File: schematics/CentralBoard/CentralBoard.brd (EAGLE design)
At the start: 100 x 80 mm, 10 parts, among them CON1 XT30UPB-M, CON3 XT30UPB-M, IC1 7805T

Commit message: Starting schematics
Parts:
- removed JP1: OD0_Serial, adafruit:1X03
- added C10, C11, C12, C13, C14, C15, C9: 2.2uF, rcl:C1206
- added C17, C2, C4, C7: 100nF, rcl:C0805
- added CON2, CON4, CON5, CON6, CON7, CON8: XT30UPB-M, amass:XT30UPB-M
- added F1: Fuse 0.2A, fuse:SHK20L
- added IC2: SN75C3232, MAX3232:SOIC16
- added IC3: LTC7001, LTC7001:MSOP10
- added Q1: BC328, transistor-pnp:TO92-EBC
- added R3: 4m, rcl:R2512
- added R4: 10K, rcl:R0805
- added R5: 100K, rcl:R0805
- added R6, R7: 1K, rcl:R0805
- added SJ1, SJ2, SJ3, SJ4: 0, jumper:SJ
- added SV3: IMU, con-lstb:MA06-1
- added U$2: NVMFS6H824NL-D, DIO_NTS1045EMFST1G:DIO_NTS1045EMFST1G
- C1: value (none) -> 1uF; device rcl:E15-5 -> rcl:E2-5
- C3: value (none) -> 4.7uF; device rcl:E15-5 -> rcl:C0805
- C5: value (none) -> 10uF; device rcl:E2,5-7 -> rcl:E2-5
- C6: value (none) -> 0.47uF; device rcl:E2,5-7 -> rcl:C0805
- D1: device adafruit:DO41-10 -> diode:DO41-10
- IC1: value 7805T -> R-78C05.0; device adafruit:TO220H -> v-reg:78XXS
- moved CON3 166.9 mm to (12.7, 86.4)
- moved IC1 162.9 mm to (152.4, 35.6)
- moved C5 155.4 mm to (100.3, 68.6)
- moved CON1 151.8 mm to (12.7, 94.0)
- moved C6 139.3 mm to (44.5, 81.3)
- moved C1 128.1 mm to (91.4, 68.6)
- moved D1 113.7 mm to (88.9, 52.1)
- moved C3 108.6 mm to (44.5, 69.8)
- moved U$1 51.5 mm to (99.1, 17.8)
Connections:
- removed net RX1: JP1.1, U$1.0-RX1/CS1/CRX2
- removed net TX1: JP1.2, U$1.1-TX1/MISO1/CTX2
- new net +5V: C5.+, D1.A, IC1.OUT, IC3.1, Q1.E, R6.1, U$1.VIN
- new net BATT+: CON1.+, CON3.+, R3.1, SJ1.1
- new net BATT-: C10.2, C11.2, C12.2, C13.2, C14.2, C15.2, C9.2, CON1.-, CON2.-, CON3.-, CON4.-, CON5.-, CON6.-, CON7.-, CON8.-, SJ2.1, SJ4.2
- new net IMU-D+: SV3.4
- new net IMU_D-: SV3.3
- new net IMU_RX: IC2.P$14, SV3.6
- new net IMU_TX: IC2.P$13, SV3.5
- new net IMU_VDD: Q1.C, SV3.2
- new net N$1: C1.+, D1.C, F1.2A, IC1.IN
- new net N$10: IC3.4, R4.2, U$1.30-CRX3
- new net N$11: C2.1, IC2.P$4
- new net N$12: C2.2, IC2.P$5
- new net N$13: C7.1, IC2.P$2
- new net N$14: C4.1, IC2.P$6
- new net N$15: R4.1, SJ4.1
- new net N$16: C3.1, IC3.9
- new net N$17: IC3.7, R5.2
- new net N$18: R3.2, U$2.5_6
- new net N$19: C6.1, IC3.6, R5.1, U$2.4
- new net N$2: IC2.P$11, U$1.29-TX7
- new net N$20: F1.1A, SJ1.2
- new net N$21: C10.1, C11.1, C12.1, C13.1, C14.1, C15.1, C9.1, CON2.+, CON4.+, CON5.+, CON6.+, CON7.+, CON8.+, SJ3.2, U$2.1, U$2.2, U$2.3
- new net N$5: IC2.P$12, U$1.28-RX7
- new net N$6: C17.1, IC2.P$1
- new net N$7: R6.2, R7.1, U$1.10-CS\MQSR
- new net N$8: C17.2, IC2.P$3
- new net N$9: IC2.P$16, U$1.3V3-3
- net GND: now also C4.2, C7.2, IC1.GND, IC2.P$15, IC3.11, IC3.2, IC3.3, IC3.5, SJ2.2, SV3.1; no longer C3.-, C6.-, CON1.-, CON3.-, IC1.2, JP1.3
- net N$3: now also Q1.B, R7.2; no longer C1.+, C5.+, D1.A, IC1.3, U$1.VIN
- net N$4: now also C3.2, C6.2, IC3.8, SJ3.1; no longer C3.+, C6.+, CON1.+, CON3.+, D1.C, IC1.1
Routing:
- net GND: track 0.00 -> 294.1 mm, vias 0 -> 1
- net +5V: track 0.00 -> 195.5 mm, vias 0 -> 2
- net N$1: track 0.00 -> 134.0 mm
- net BATT-: track 0.00 -> 122.2 mm
- net N$10: track 0.00 -> 103.4 mm, vias 0 -> 1
- net N$20: track 0.00 -> 92.3 mm
- net N$21: track 0.00 -> 86.9 mm, vias 0 -> 1
- net N$7: track 0.00 -> 81.7 mm
- net N$3: track 0.00 -> 70.4 mm
- net N$6: track 0.00 -> 67.2 mm, vias 0 -> 2
- net N$8: track 0.00 -> 66.9 mm, vias 0 -> 2
- net N$13: track 0.00 -> 48.2 mm, vias 0 -> 2
- net N$15: track 0.00 -> 46.4 mm
- net N$5: track 0.00 -> 41.9 mm
- net N$19: track 0.00 -> 40.5 mm
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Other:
- board size 100 x 80 mm -> 160 x 100 mm

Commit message: used MAX3232 IC for IMU connection now
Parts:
- removed C3: 4.7uF, rcl:C0805
- removed F1: Fuse 0.2A, fuse:SHK20L
- removed IC3: LTC7001, LTC7001:MSOP10
- removed R5: 100K, rcl:R0805
- removed R6: 1K, rcl:R0805
- added D2: 1N4148DO35-7, diode:DO35-7
- added R1: 10k, rcl:R0805
- added U1: LTC4440ES6-5TRMSOP8P, LTC4440ES6-5TR:MSOP8P
- U$2: value NVMFS6H824NL-D -> DMTH8003SPS
- moved C17 59.9 mm to (104.1, 33.0)
- moved C7 54.6 mm to (99.1, 33.0)
- moved Q1 17.7 mm to (150.5, 48.9)
- moved IC1 11.8 mm to (142.9, 42.5)
- moved C4 5.24 mm to (114.3, 33.0)
- moved IC2 2.54 mm to (106.7, 40.6)
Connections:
- removed net N$16: C3.1, IC3.9
- removed net N$17: IC3.7, R5.2
- new net N$24: C6.1, D2.C, U1.6
- net +5V: now also D2.A, R1.1, U1.3; no longer IC3.1, R6.1
- net GND: no longer IC3.11, IC3.2, IC3.3, IC3.5
- net N$1: no longer F1.2A
- net N$10: now also U1.1; no longer IC3.4
- net N$15: now also U1.2, U1.4, U1.9
- net N$19: now also U1.7; no longer C6.1, IC3.6, R5.1
- net N$20: no longer F1.1A
- net N$3: now also R1.2
- net N$4: now also U1.8; no longer C3.2, IC3.8
- net N$7: now also U$1.9-OUT1C; no longer R6.2, U$1.10-CS\MQSR
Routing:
- net GND: track 294.1 -> 0.00 mm, vias 1 -> 0
- net +5V: track 195.5 -> 0.00 mm, vias 2 -> 0
- net N$1: track 134.0 -> 0.00 mm
- net BATT-: track 122.2 -> 0.00 mm
- net N$10: track 103.4 -> 0.00 mm, vias 1 -> 0
- net N$20: track 92.3 -> 0.00 mm
- net N$21: track 86.9 -> 0.00 mm, vias 1 -> 0
- net N$7: track 81.7 -> 0.00 mm
- net N$3: track 70.4 -> 0.00 mm
- net N$6: track 67.2 -> 0.00 mm, vias 2 -> 0
- net N$8: track 66.9 -> 0.00 mm, vias 2 -> 0
- net N$13: track 48.2 -> 0.00 mm, vias 2 -> 0
- net N$15: track 46.4 -> 0.00 mm
- net N$5: track 41.9 -> 0.00 mm
- net N$19: track 40.5 -> 0.00 mm
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
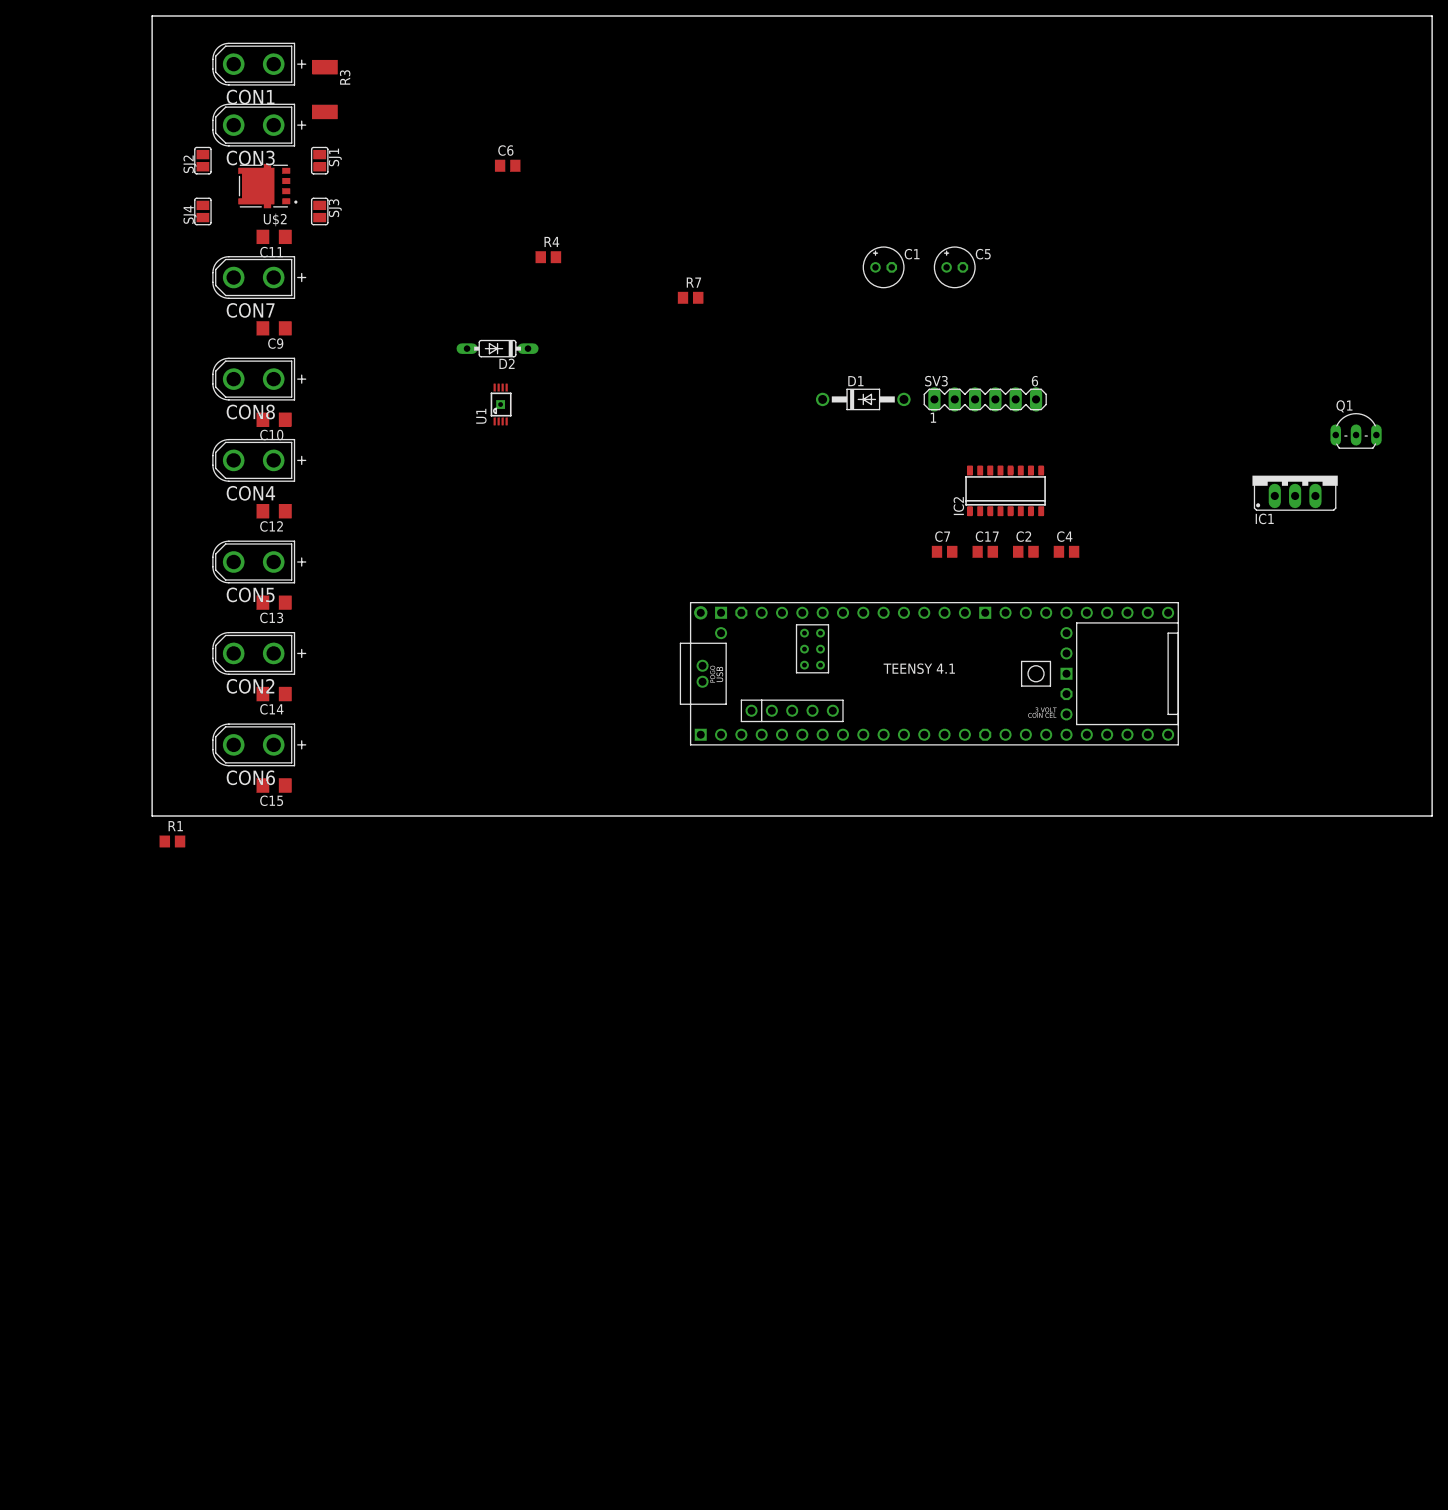
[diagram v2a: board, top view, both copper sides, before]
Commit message: Added sockets for IMU, Sensors and ODrives
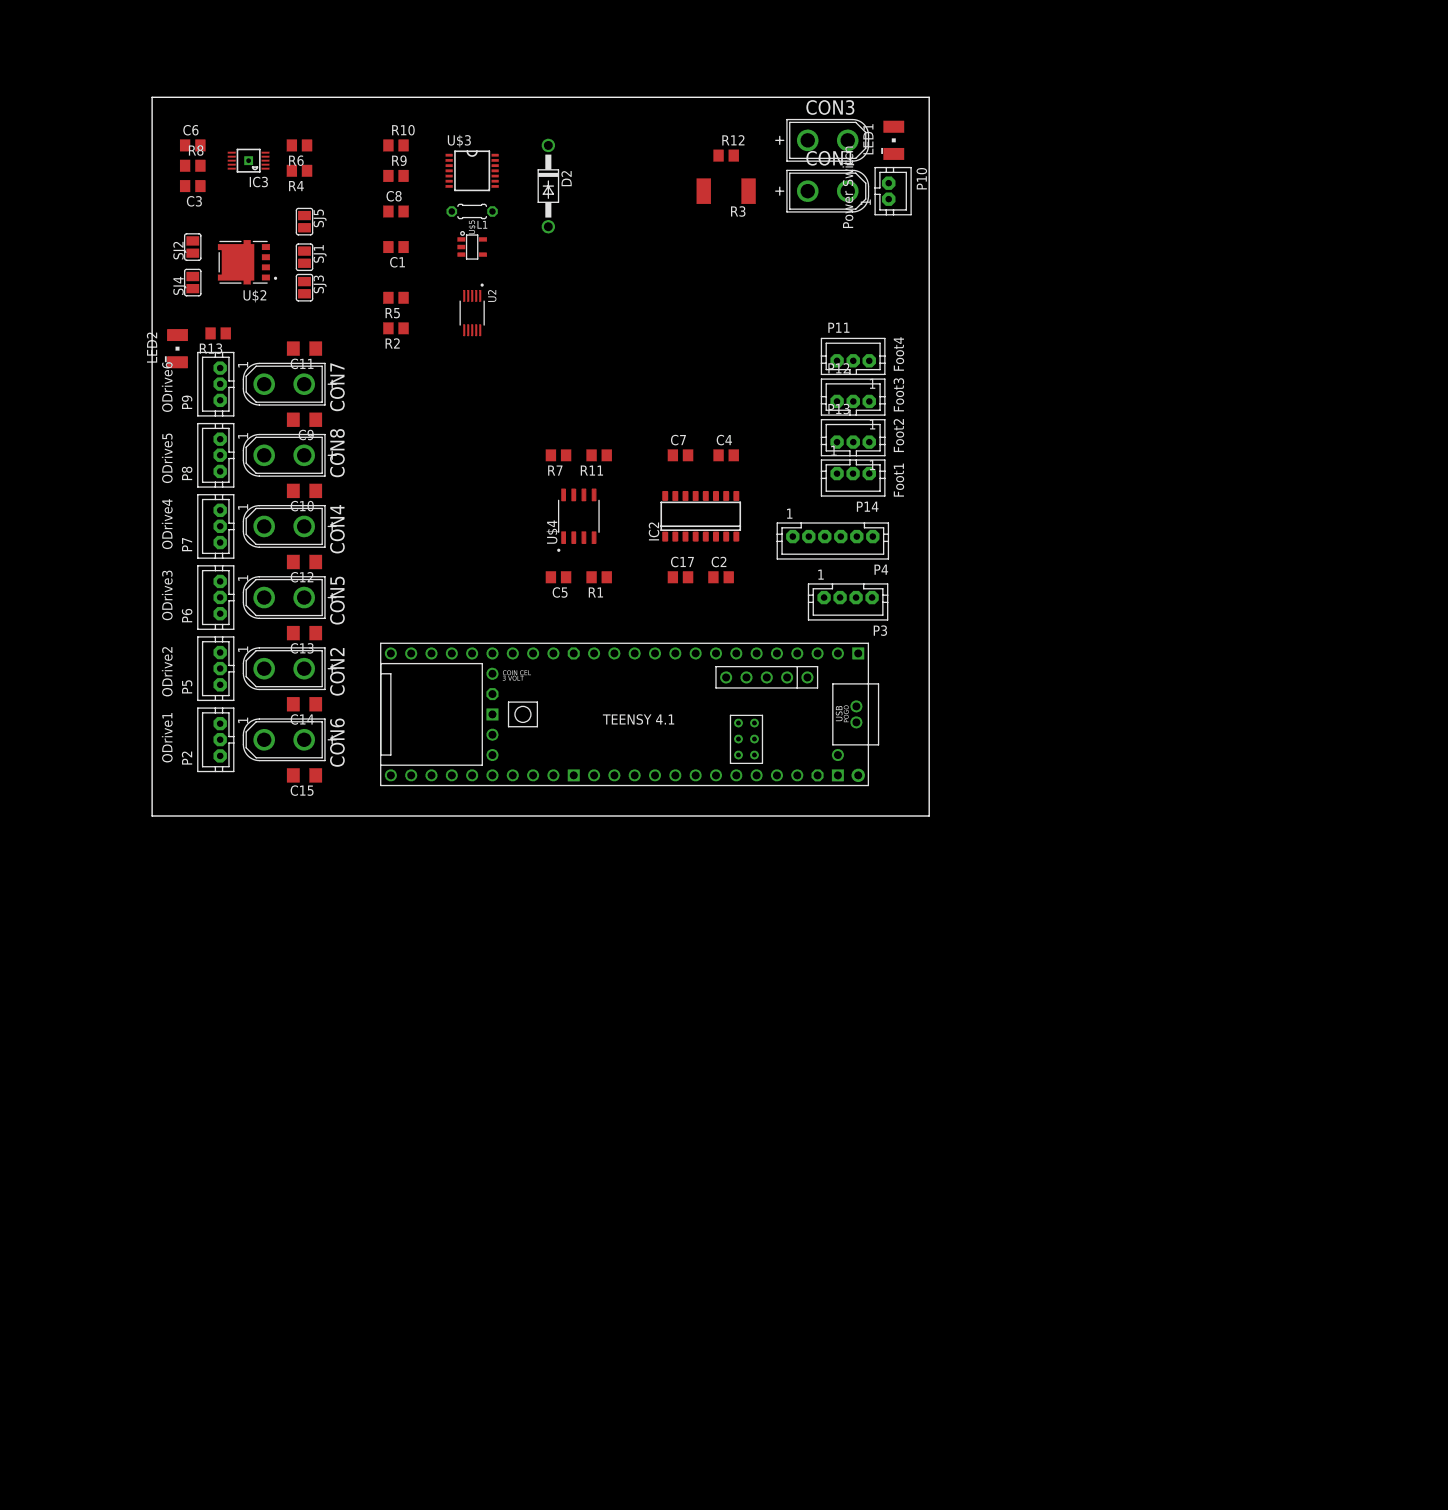
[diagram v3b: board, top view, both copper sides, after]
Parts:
- removed D1: 1N4004, diode:DO41-10
- removed IC1: R-78C05.0, v-reg:78XXS
- removed Q1: BC328, transistor-pnp:TO92-EBC
- removed SV3: IMU, con-lstb:MA06-1
- removed U1: LTC4440ES6-5TRMSOP8P, LTC4440ES6-5TR:MSOP8P
- added C3: 4.7uF, rcl:C0805
- added C8: 10uF, rcl:C0805
- added IC3: LTC7001, LTC7001:MSOP10
- added L1: 10uH, rcl:0204/5
- added LED1: Power, led:PLCC2
- added LED2: P-ODrive, led:PLCC2
- added P10: Power Switch, jst-ph:JST-PH2
- added P11: Foot4, jst-ph:JST-PH3
- added P12: Foot3, jst-ph:JST-PH3
- added P13: Foot2, jst-ph:JST-PH3
- added P14: Foot1, jst-ph:JST-PH3
- added P2: ODrive1, jst-ph:JST-PH3
- added P3: MAIN_SPI, jst-ph:JST-PH4
- added P4: IMU, jst-ph:JST-PH6
- added P5: ODrive2, jst-ph:JST-PH3
- added P6: ODrive3, jst-ph:JST-PH3
- added P7: ODrive4, jst-ph:JST-PH3
- added P8: ODrive5, jst-ph:JST-PH3
- added P9: ODrive6, jst-ph:JST-PH3
- added R10: 100k, rcl:R0805
- added R11, R8: 100K, rcl:R0805
- added R12, R13: 1K, rcl:R0805
- added R2, R5: 2.2K, rcl:R0805
- added R6: 10K, rcl:R0805
- added R9: 47k, rcl:R0805
- added SJ5: 0, jumper:SJ
- added U$3: TLF50211EL, TLF50211EL:TSSOP-14
- added U$4: MCP1725-ADJE/SN, MCP1725-ADJE_SN:SOIC127P599X175-8N
- added U$5: AP2128-3.3V, AP2128:SOT-23-5
- added U2: INA226AIDGST, INA226AIDGST:SOP50P490X110-10N
- C1: device rcl:E2-5 -> rcl:C0805
- C5: value 10uF -> 1nF; device rcl:E2-5 -> rcl:C0805
- D2: value 1N4148DO35-7 -> 1N4004; device diode:DO35-7 -> diode:DO41-10
- R1: value 10k -> 100K
- R7: value 1K -> 10K
- moved CON1 73.5 mm to (84.5, 78.1), turned to 180 degrees
- moved CON3 71.8 mm to (84.5, 84.5), turned to 180 degrees
- moved C5 62.9 mm to (50.8, 29.8), turned to 180 degrees
- moved R1 62.7 mm to (55.9, 29.8), turned to 180 degrees
- moved C1 61.0 mm to (30.5, 71.1), turned to 180 degrees
- moved R3 51.7 mm to (71.8, 78.1), turned to 180 degrees
- moved C4 44.2 mm to (71.8, 45.1)
- moved U$1 41.6 mm to (57.8, 12.7), turned to 180 degrees
- moved C6 39.5 mm to (5.08, 83.8)
- moved IC2 38.2 mm to (68.6, 37.5)
- moved C17 38.2 mm to (66.0, 29.8)
- moved C2 38.2 mm to (71.1, 29.8)
- moved C7 35.2 mm to (66.0, 45.1)
- moved R4 32.9 mm to (18.4, 80.6), turned to 180 degrees
- moved R7 25.7 mm to (50.8, 45.1), turned to 180 degrees
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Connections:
- net N$2 renamed T_TX
- net N$5 renamed T_RX
- new net +3.3V: C1.1, P11.2, P12.2, P13.2, P14.2, U$5.4
- new net BATT: P10.1, SJ1.2, U$3.13, U2.10, U2.8
- new net CS: P3.4, U$1.10-CS\MQSR
- new net MISO: P3.2, U$1.12-MISO/MQSL
- new net MOSI: P3.3, U$1.11-MOSI/CTX1
- new net N$16: C6.2, R6.2
- new net N$17: R2.1, U$1.19-A5/SCL0, U2.5
- new net N$2: LED1.C, R12.2
- new net N$22: R5.1, U$1.18-A4/SDA0, U2.4
- new net N$23: R11.2, R2.2, R5.2, U$1.3V3-3, U2.6
- new net N$25: R1.1, R7.2, U$4.7
- new net N$26: C3.2, IC3.8, LED2.A, SJ3.1
- new net N$27: R9.2, U$3.5
- new net N$29: D2.C, L1.1, U$3.11
- new net N$30: LED2.C, R13.2
- new net N$31: IC2.P$16, P4.5, R1.2, U$4.8
- new net N$5: U$1.31-CTX3, U2.3
- new net O1_RX: P2.2, U$1.0-RX1/CS1/CRX2
- new net O1_TX: P2.3, U$1.1-TX1/MISO1/CTX2
- new net O2_RX: P5.2, U$1.7-RX2/OUT1A
- new net O2_TX: P5.3, U$1.8-TX2/IN1
- new net O3_RX: P6.2, U$1.15-A1/RX3/SPDIF_IN
- new net O3_TX: P6.3, U$1.14-A0/TX3/SPDIF_OUT
- new net O4_RX: P7.2, U$1.16-A2/RX4/SCL1
- new net O4_TX: P7.3, U$1.17-A3/TX4/SDA1
- new net O5_RX: P8.2, U$1.21-A7/RX5/BCLK1
- new net O5_TX: P8.3, U$1.20-A6/TX5/LRCLK1
- new net O6_RX: P9.2, U$1.25-A11/RX6/SDA2
- new net O6_TX: P9.3, U$1.24-A10/TX6/SCL2
- new net SENSOR1: P14.3, U$1.22-A8/CTX1
- new net SENSOR2: P13.3, U$1.23-A9/CRX1/MCLK1
- new net SENSOR3: P12.3, U$1.38-A14/CS/IN1
- new net SENSOR4: P11.3, U$1.39-A15/CS/OUT1A
- net +5V: now also C8.1, IC3.1, L1.2, LED1.A, U$3.7, U$4.1, U$4.2, U$5.3; no longer C5.+, D1.A, D2.A, IC1.OUT, Q1.E, R1.1, U$1.VIN, U1.3
- net GND: now also C1.2, C5.2, C8.2, D2.A, P11.1, P12.1, P13.1, P14.1, P2.1, P3.1, P4.6, P5.1, P6.1, P7.1, P8.1, P9.1, R10.1, R12.1, R7.1, R9.1, U$3.10, U$3.4, U$3.9, U$4.4, U$5.2, U2.1, U2.2, U2.7; no longer C1.-, C5.-, IC1.GND, SV3.1
- net IMU-D+: now also P4.3; no longer SV3.4
- net IMU_D-: now also P4.4; no longer SV3.3
- net IMU_RX: now also P4.1; no longer SV3.6
- net IMU_TX: now also P4.2; no longer SV3.5
- net IMU_VDD: now also R11.1, U$1.32-OUT1B, U$4.5; no longer Q1.C, SV3.2
- net N$1: now also U$1.VIN; no longer C1.+, D1.C, IC1.IN
- net N$10: now also IC3.4; no longer U1.1
- net N$15: now also IC3.11, IC3.2, IC3.3, IC3.5, R13.1, R6.1; no longer U1.2, U1.4, U1.9
- net N$18: now also SJ5.1, U2.9; no longer R3.2, U$2.5_6
- net N$19: now also C6.1, IC3.6, R8.1; no longer U1.7
- net N$20: now also P10.2, R10.2, U$3.14; no longer SJ1.2
- net N$24: now also C3.1, IC3.9; no longer C6.1, D2.C, U1.6
- net N$3: now also C5.1, U$4.6; no longer Q1.B, R1.2, R7.2
- net N$4: now also IC3.7, R8.2; no longer C6.2, SJ3.1, U1.8
- net N$7: now also U$4.3; no longer R7.1
- net N$9: now also R3.2, SJ5.2, U$2.5_6; no longer IC2.P$16, U$1.3V3-3
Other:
- board size 160 x 100 mm -> 97.1 x 89.8 mm
